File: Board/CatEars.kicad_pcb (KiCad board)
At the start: 2 copper layers, 65.1 x 39 mm, 43 parts, among them J31 Conn_01x01, J32 Conn_01x01, U2 AP2112K-3.3

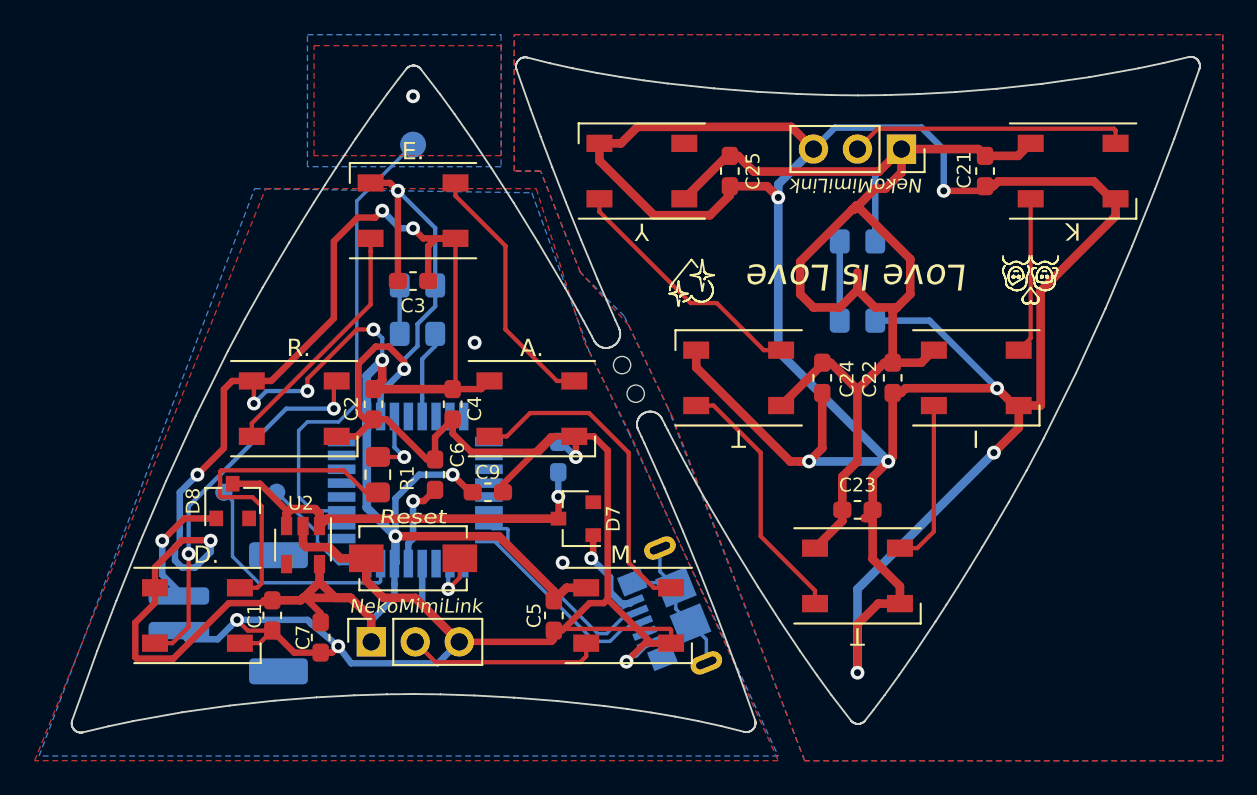
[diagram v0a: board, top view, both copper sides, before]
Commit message: Minor board design revision to allow more space to connect battery and easier assembly
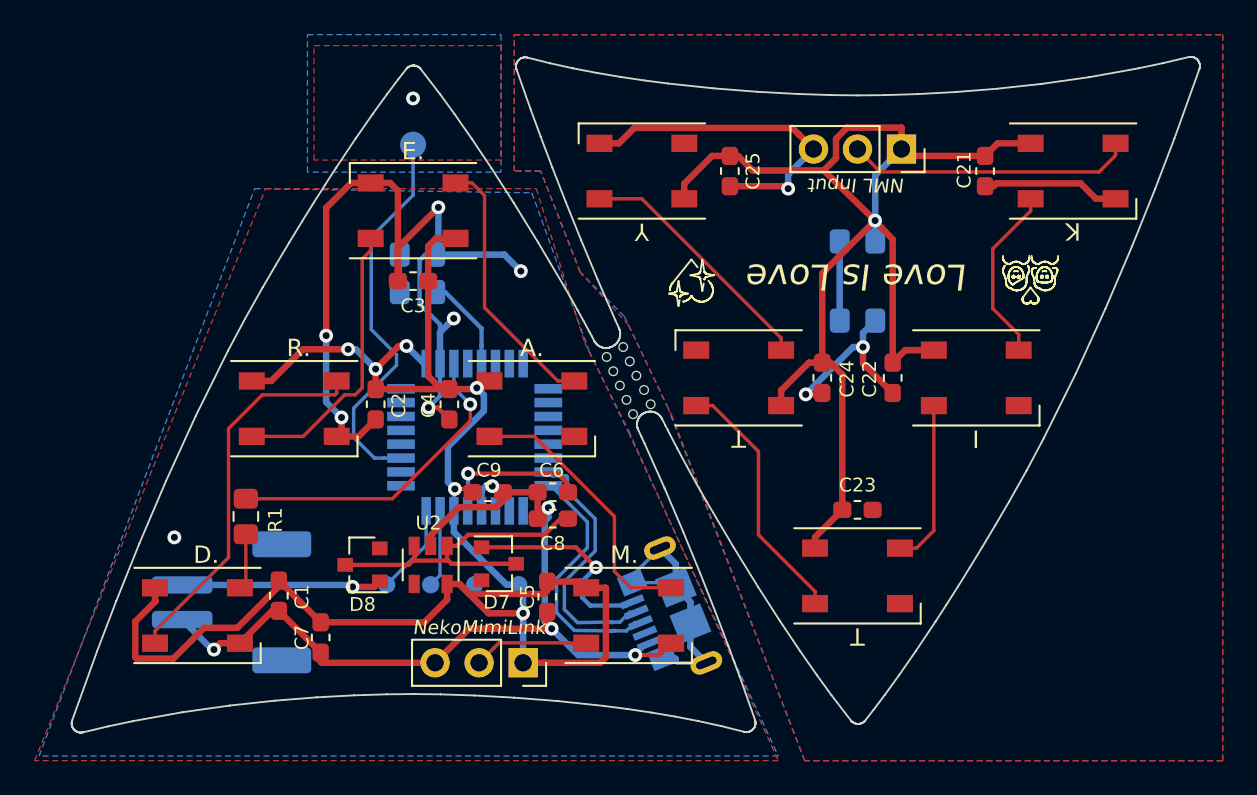
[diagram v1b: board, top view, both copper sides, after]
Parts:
- removed the REF** at (231.5, 135.0)
- removed the REF** at (230.8, 133.4)
- removed Reset: SW_Push, Button_Switch_SMD:SW_SPST_EVQPE1
- added 3V3: Conn_01x01, TestPoint:TestPoint_Pad_D1.0mm, B.Cu at (224.8, 146.1)
- added GND: Conn_01x01, TestPoint:TestPoint_Pad_D1.0mm, B.Cu at (222.2, 146.1)
- added REF**: 1mm_npth, footprints:1mm_npth, F.Cu at (232.4, 135.6)
- added REF**: 1mm_npth, footprints:1mm_npth, F.Cu at (229.9, 132.9)
- added REF**: 1mm_npth, footprints:1mm_npth, F.Cu at (232.0, 134.8)
- added REF**: 1mm_npth, footprints:1mm_npth, F.Cu at (231.6, 134.0)
- added REF**: 1mm_npth, footprints:1mm_npth, F.Cu at (231.2, 133.2)
- added REF**: 1mm_npth, footprints:1mm_npth, F.Cu at (230.8, 132.3)
- added REF**: 1mm_npth, footprints:1mm_npth, F.Cu at (231.4, 136.2)
- added REF**: 1mm_npth, footprints:1mm_npth, F.Cu at (231.0, 135.4)
- added REF**: 1mm_npth, footprints:1mm_npth, F.Cu at (230.6, 134.6)
- added REF**: 1mm_npth, footprints:1mm_npth, F.Cu at (230.3, 133.7)
- ATSAMD21E18: renamed from Microcontroller :D
- C8: moved to F.Cu
- NML Input: renamed from NekoMimiLink
- moved 31 13.1 mm to (219.7, 146.1)
- moved NekoMimiLink 8.85 mm to (225.0, 150.6), turned to 270 degrees
- moved D8 8.35 mm to (215.8, 144.9), turned to 180 degrees
- moved 32 8.29 mm to (217.2, 146.1)
- moved R1 7.99 mm to (209.0, 142.1)
- moved U2 7.45 mm to (219.7, 144.9)
- moved C6 6.87 mm to (226.8, 140.7), turned to 0 degrees
- moved D7 5.15 mm to (223.6, 144.8), turned to 0 degrees
- moved ATSAMD21E18 4.59 mm to (222.2, 137.5)
- moved C8 3.57 mm to (226.8, 142.2), turned to 180 degrees
- moved R6 2.41 mm to (218.9, 129.2)
- moved D6 1.78 mm to (218.9, 127.0)
- moved C1 1.20 mm to (210.9, 146.7)
- moved C5 1.14 mm to (226.4, 146.7)
- moved BT1 0.66 mm to (208.2, 147.1)
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- renumbered J31 to 31, J32 to 32, Battery! to BT1, Power! to D0
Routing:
- net Net-(C21-Pad2): track 158.5 -> 38.1 mm, vias 7 -> 3
- net +3V3: track 140.5 -> 101.8 mm, vias 10 -> 6
- net GND: track 138.5 -> 110.2 mm, vias 8 -> 12
- net Net-(D1-Pad4): track 19.5 -> 3.37 mm
- net Net-(R1-Pad1): track 4.11 -> 18.5 mm
- net Net-(J31-Pad1): track 14.1 -> 4.48 mm
- net Net-(C21-Pad1): track 80.1 -> 72.1 mm, vias 0 -> 1
- net VBUS: track 5.36 -> 12.3 mm
- net Net-(C8-Pad1): track 24.9 -> 19.4 mm, vias 1 -> 0
- net Net-(D5-Pad2): track 11.3 -> 6.67 mm
- net +BATT: track 7.34 -> 11.6 mm
- net Net-(H1-Pad1): track 26.9 -> 22.8 mm
- net /USB_D-: track 11.7 -> 15.3 mm
- net Net-(SW1-Pad1): track 3.56 -> 0.00 mm, vias 1 -> 0
- net Net-(C6-Pad2): track 5.27 -> 8.65 mm
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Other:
- board text added: "+"
- board text added: "-"
- board text added: "Meow Meow Ears v3b by @GalaxyAllieCat 2020-03-01"
- board text removed: "Meow Meow Ears v3 by @GalaxyAllieCat 2020-02-06"

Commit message: tiny tweaks, added new link + battery discharge warning
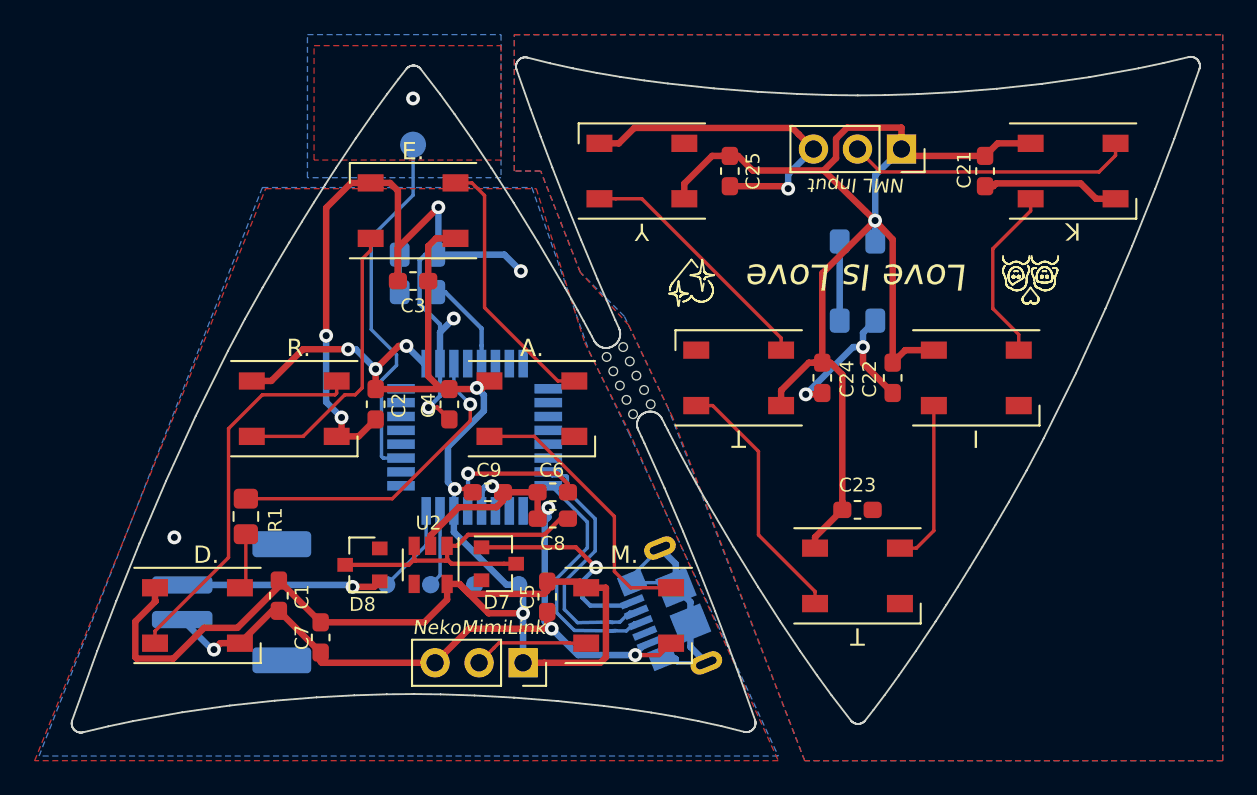
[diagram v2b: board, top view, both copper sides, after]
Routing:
- net Net-(H1-Pad1): track 22.8 -> 21.1 mm
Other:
- board text added: "Meow Meow Ears v3b by @GalaxyAllieCat 2020-03-02"
- board text removed: "Meow Meow Ears v3b by @GalaxyAllieCat 2020-03-01"
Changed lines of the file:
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@@
     (thickness 1.6)
     (drawings 6414)
-    (tracks 366)
+    (tracks 367)
     (zones 0)
     (modules 52)
@@
     (44 Edge.Cuts user)
     (45 Margin user hide)
-    (46 B.CrtYd user)
+    (46 B.CrtYd user hide)
     (47 F.CrtYd user)
     (48 B.Fab user hide)
@@
   )
   (setup
-    (last_trace_width 0.375)
+    (last_trace_width 0.2)
     (user_trace_width 0.2)
     (user_trace_width 0.375)
@@
   (gr_line (start 253.724214 129.038497) (end 253.702066 129.044269) (layer F.SilkS) (width 0.105833))
   (gr_line (start 253.746 129.032) (end 253.724214 129.038497) (layer F.SilkS) (width 0.105833))
-  (gr_text "Meow Meow Ears v3b\nby @GalaxyAllieCat\n2020-03-01" (at 212.344 132.08 60) (layer B.SilkS)
+  (gr_text "Meow Meow Ears v3b\nby @GalaxyAllieCat\n2020-03-02" (at 212.344 132.08 60) (layer B.SilkS)
     (effects (font (size 1 1) (thickness 0.15) italic) (justify mirror))
   )
@@
   (segment (start 216.281 125.984) (end 216.281 131.318) (width 0.2) (layer B.Cu) (net 6))
   (segment (start 216.281 131.318) (end 217.7415 132.7785) (width 0.2) (layer B.Cu) (net 6))
-  (segment (start 217.7415 133.384498) (end 215.265 135.860998) (width 0.2) (layer B.Cu) (net 6))
   (segment (start 217.7415 132.7785) (end 217.7415 133.384498) (width 0.2) (layer B.Cu) (net 6))
-  (segment (start 217 138.741) (end 218 138.741) (width 0.2) (layer B.Cu) (net 6))
-  (segment (start 216.465 138.741) (end 217 138.741) (width 0.2) (layer B.Cu) (net 6))
-  (segment (start 215.265 135.860998) (end 215.265 137.541) (width 0.2) (layer B.Cu) (net 6))
-  (segment (start 215.265 137.541) (end 216.465 138.741) (width 0.2) (layer B.Cu) (net 6))
   (via (at 218.694 117.983) (size 0.8) (drill 0.4) (layers F.Cu B.Cu) (net 6))
+  (segment (start 217 138.741) (end 216.9935 138.7475) (width 0.2) (layer B.Cu) (net 6))
+  (segment (start 218 138.741) (end 217 138.741) (width 0.2) (layer B.Cu) (net 6))
+  (segment (start 216.9935 138.7475) (end 216.9795 138.7475) (width 0.2) (layer B.Cu) (net 6))
+  (segment (start 216.869525 134.256473) (end 217.7415 133.384498) (width 0.2) (layer B.Cu) (net 6))
+  (segment (start 216.9795 138.7475) (end 216.869525 138.637525) (width 0.2) (layer B.Cu) (net 6))
+  (segment (start 216.869525 138.637525) (end 216.869525 134.256473) (width 0.2) (layer B.Cu) (net 6))
   (segment (start 233.590576 145.935778) (end 233.863188 146.20839) (width 0.2) (layer B.Cu) (net 7))
   (segment (start 231.347913 145.935778) (end 233.590576 145.935778) (width 0.2) (layer B.Cu) (net 7))
@@
     (polygon
       (pts
-        (xy 225.552 123.429509) (xy 228.854 132.573509) (xy 231.14 137.272509) (xy 239.776 155.941509) (xy 197.104 155.941509)
-        (xy 209.55 123.19)
+        (xy 225.552 123.1265) (xy 228.854 132.573509) (xy 231.14 137.272509) (xy 239.776 155.941509) (xy 197.104 155.941509)
+        (xy 209.9945 123.1265)
       )
     )
@@
     (polygon
       (pts
-        (xy 223.774 122.2375) (xy 212.598 122.2375) (xy 212.598 114.3) (xy 223.774 114.3)
+        (xy 223.774 122.555) (xy 212.598 122.555) (xy 212.598 114.3) (xy 223.774 114.3)
       )
     )
